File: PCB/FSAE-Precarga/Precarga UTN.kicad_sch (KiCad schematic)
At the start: 64 parts, among them J1 TS+, J3 Conn_02x05_Counter_Clockwise, J4 Conn_01x02_Pin, J5 RA+_Control, J6 RA-_Control, J7 TS-, SW1 SW_MEC_5E, U1 TMA-1212S, U2 LM331N, U3 6N137, U4 6N137, U5 LM331N, U6 STM32F103C8Tx, U7 LM1117DT-3.3, Y1 Crystal

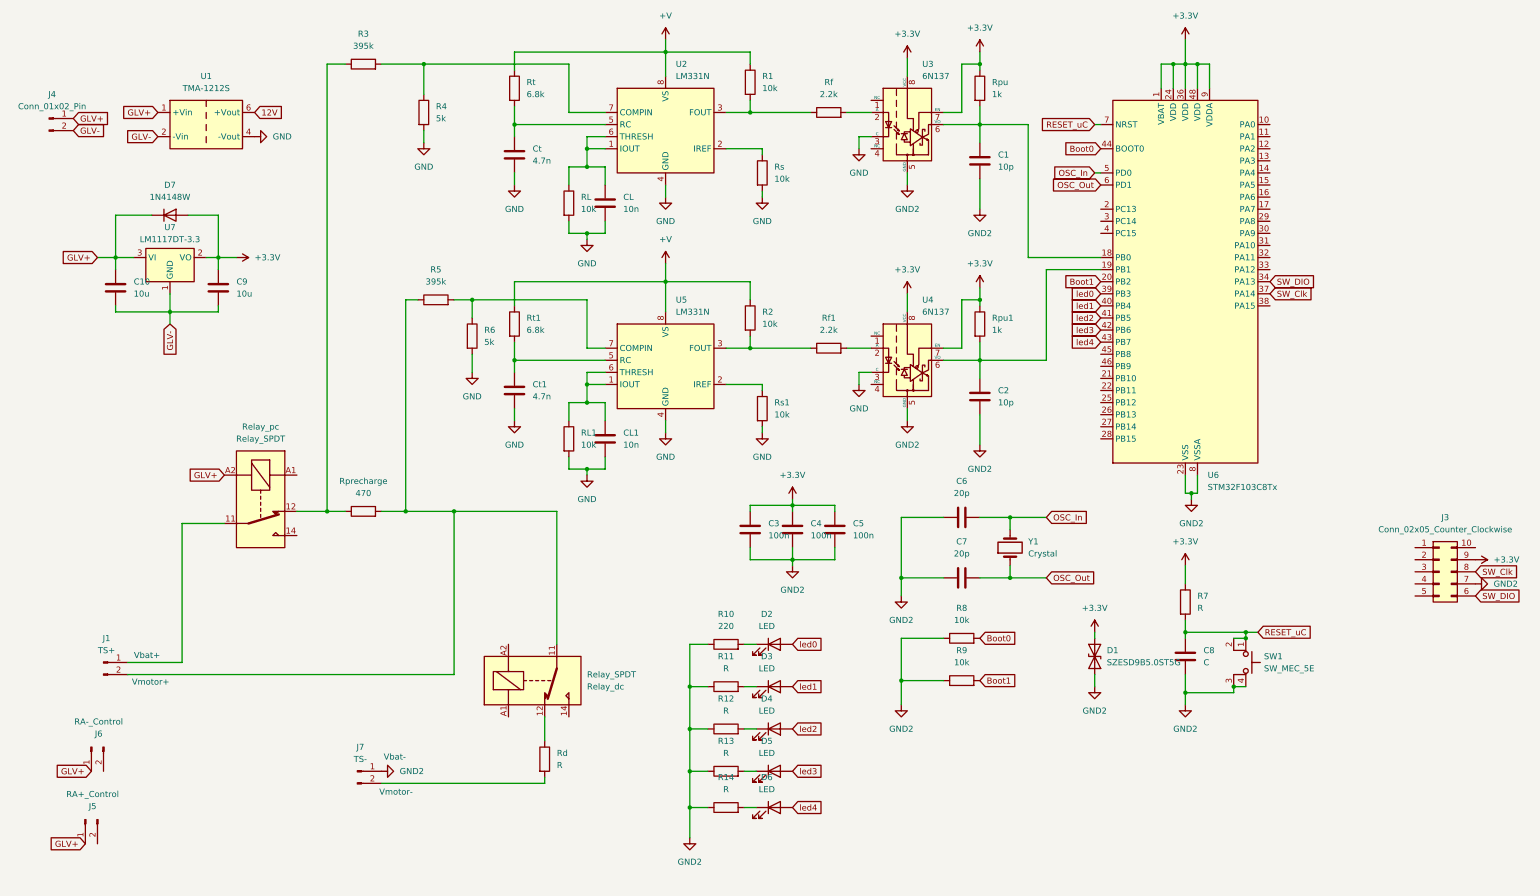
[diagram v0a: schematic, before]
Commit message: Version avanzada (NO final) de la placa de precarga
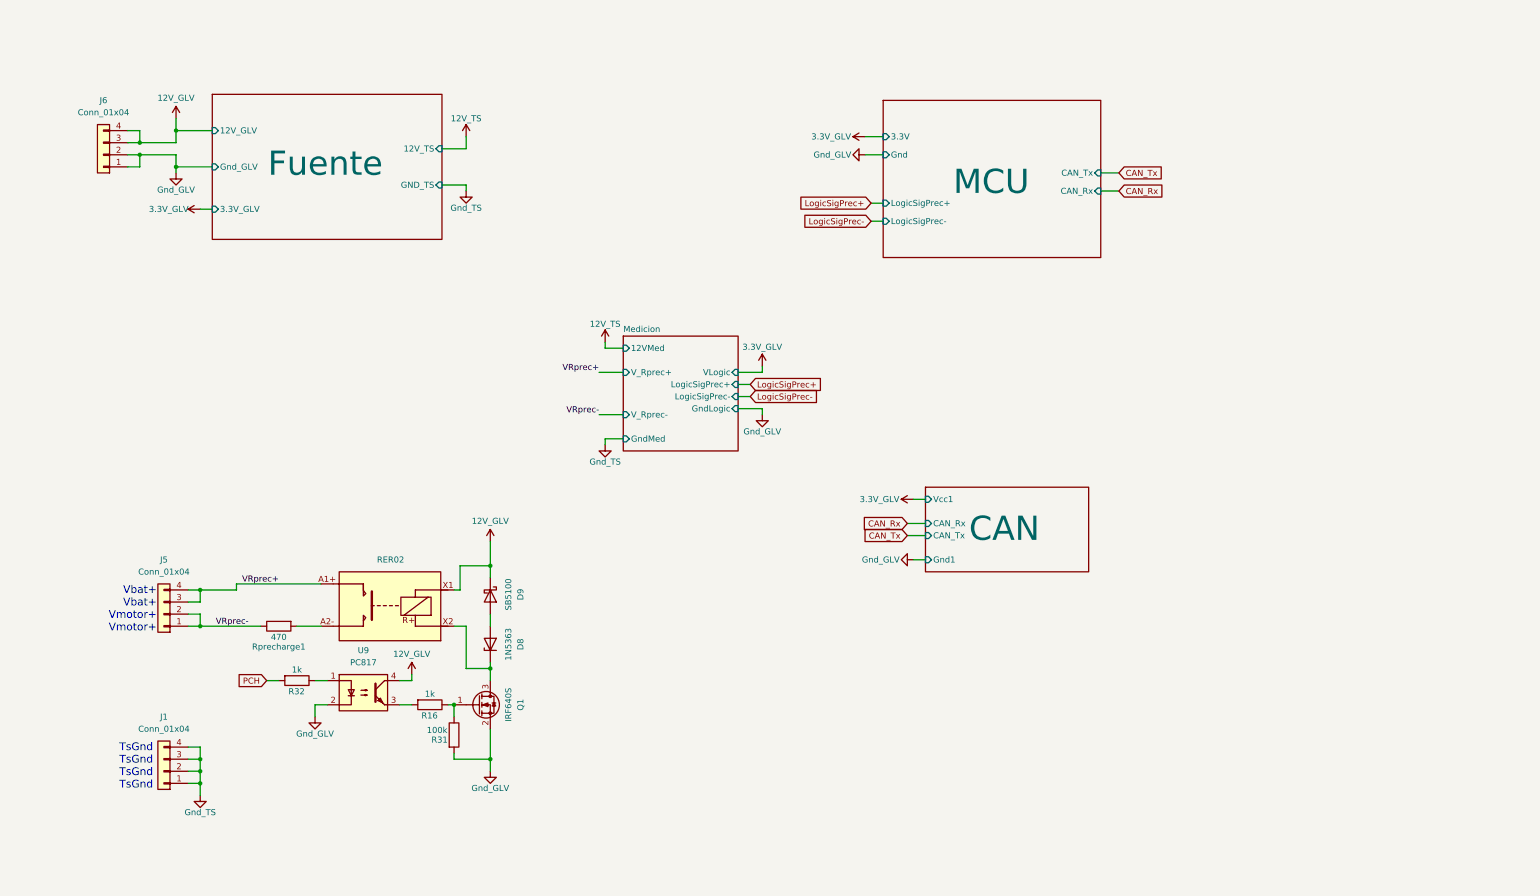
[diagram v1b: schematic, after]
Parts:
- removed C1, C2: 10p, symbol Device:C
- removed C10, C9: 10u, symbol Device:C
- removed C3, C4, C5: 100n, symbol Device:C
- removed C6, C7: 20p, symbol Device:C
- removed C8: C, symbol Device:C
- removed CL, CL1: 10n, symbol Device:C
- removed Ct, Ct1: 4.7n, symbol Device:C
- removed D1: SZESD9B5.0ST5G, Diode_SMD:D_SOD-923, symbol Diode:SZESD9B5.0ST5G
- removed D2, D3, D4, D5, D6: LED, symbol Device:LED
- removed D7: 1N4148W, Diode_SMD:D_SOD-123, symbol Diode:1N4148W
- removed J1: TS+, symbol Connector:Conn_01x02_Pin
- removed J3: Conn_02x05_Counter_Clockwise, Connector_IDC:IDC-Header_2x05_P2.54mm_Vertical, symbol Connector_Generic:Conn_02x05_Counter_Clockwise
- removed J4: Conn_01x02_Pin, symbol Connector:Conn_01x02_Pin
- removed J5: RA+_Control, symbol Connector:Conn_01x02_Pin
- removed J6: RA-_Control, symbol Connector:Conn_01x02_Pin
- removed J7: TS-, symbol Connector:Conn_01x02_Pin
- removed R1, R2, R8, R9, RL, RL1, Rs, Rs1: 10k, symbol Device:R
- removed R10: 220, symbol Device:R
- removed R11, R12, R13, R14, R7, Rd: R, symbol Device:R
- removed R3, R5: 395k, symbol Device:R
- removed R4, R6: 5k, symbol Device:R
- removed Relay_dc, Relay_pc: Relay_SPDT, symbol Relay:Relay_SPDT
- removed Rf, Rf1: 2.2k, symbol Device:R
- removed Rpu, Rpu1: 1k, symbol Device:R
- removed Rt, Rt1: 6.8k, symbol Device:R
- removed SW1: SW_MEC_5E, symbol Switch:SW_MEC_5E
- removed U1: TMA-1212S, Converter_DCDC:Converter_DCDC_TRACO_TMA-05xxS_12xxS_Single_THT, symbol Converter_DCDC:TMA-1212S
- removed U2, U5: LM331N, Package_DIP:SMDIP-8_W7.62mm, symbol Analog:LM331N
- removed U3, U4: 6N137, Package_DIP:SMDIP-8_W7.62mm, symbol Isolator:6N137
- removed U6: STM32F103C8Tx, Package_QFP:LQFP-48_7x7mm_P0.5mm, symbol MCU_ST_STM32F1:STM32F103C8Tx
- removed U7: LM1117DT-3.3, Package_TO_SOT_SMD:TO-252-2, symbol Regulator_Linear:LM1117DT-3.3
- removed Y1: Crystal, symbol Device:Crystal
- added D8: 1N5363, Diode_THT:D_DO-41_SOD81_P10.16mm_Horizontal, symbol Diode:1N53xxB
- added D9: SB5100, Diode_THT:D_DO-41_SOD81_P10.16mm_Horizontal, symbol Diode:SB5H100
- added J1, J5, J6: Conn_01x04, GeneratedConnector:Molex_Mini50, symbol Connector_Generic:Conn_01x04
- added K1: RER02, Mis_Huellas:RER02PAX, symbol MisSimbolos:RER02-Series
- added Q1: IRF640S, Package_TO_SOT_SMD:TO-263-2, symbol Transistor_FET:AO3400A
- added R16, R32: 1k, Resistor_SMD:R_0603_1608Metric, symbol Device:R
- added R31: 100k, Resistor_SMD:R_0603_1608Metric, symbol Device:R
- added U9: PC817, Package_DIP:DIP-4_W7.62mm_SMDSocket_SmallPads, symbol Isolator:PC817
- Rprecharge1: renamed from Rprecharge; PaginaProveedor (none) -> https://www.digikey.com/es/products/detail/ohmite/HS25-470R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
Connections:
- net VRprec-: now reaches Rprecharge1.1
- net VRprec-: now also J5.1 (Pin_1), J5.2 (Pin_2)
- net at Rprecharge1.2: now also K1.A2-
- new net: D8.1 (K), K1.X2, Q1.3 (D)
- new net: D8.2 (A), D9.2 (A)
- new net: R32.1, U9.1
- new net: Q1.1 (G), R16.1, R31.1
- new net: R16.2, U9.3
- new net 12V_GLV: D9.1 (K), J6.3 (Pin_3), J6.4 (Pin_4), K1.X1, U9.4
- new net Gnd_GLV: J6.1 (Pin_1), J6.2 (Pin_2), Q1.2 (S), R31.2, U9.2
- new net Gnd_TS: J1.1 (Pin_1), J1.2 (Pin_2), J1.3 (Pin_3), J1.4 (Pin_4)
- new net PCH: R32.2
- new net VRprec+: J5.3 (Pin_3), J5.4 (Pin_4), K1.A1+
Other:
- added sheet CAN (CANModule.kicad_sch)
- added sheet Fuente (Fuente.kicad_sch)
- added sheet MCU (mcu.kicad_sch)
- added sheet Medicion (Medicion.kicad_sch)
- note added: "TsGnd TsGnd TsGnd TsGnd"
- note added: "Vbat+ Vbat+ Vmotor+ Vmotor+"
- note removed: "Vbat+"
- note removed: "Vbat-"
- note removed: "Vmotor+"
- note removed: "Vmotor-"
- company: (none) -> UTN-FRBA-FSAE
- title: (none) -> SistemaCarga
- moved on the sheet: Rprecharge1

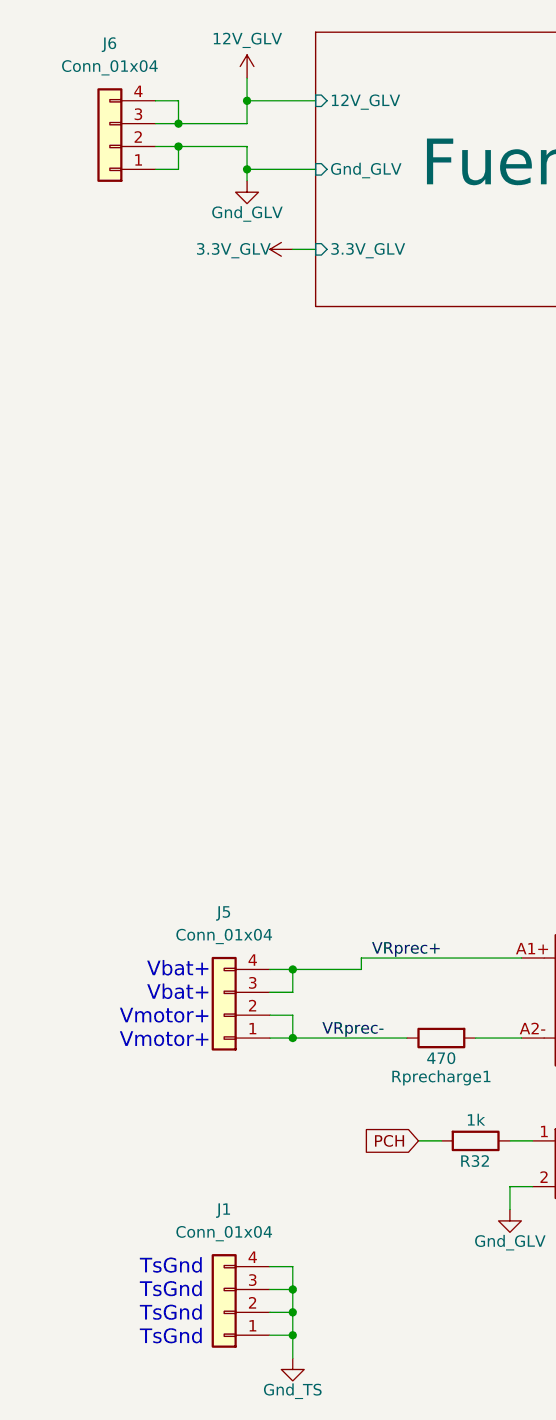
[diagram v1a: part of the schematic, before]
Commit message: Version avanzada de la placa de Precarga
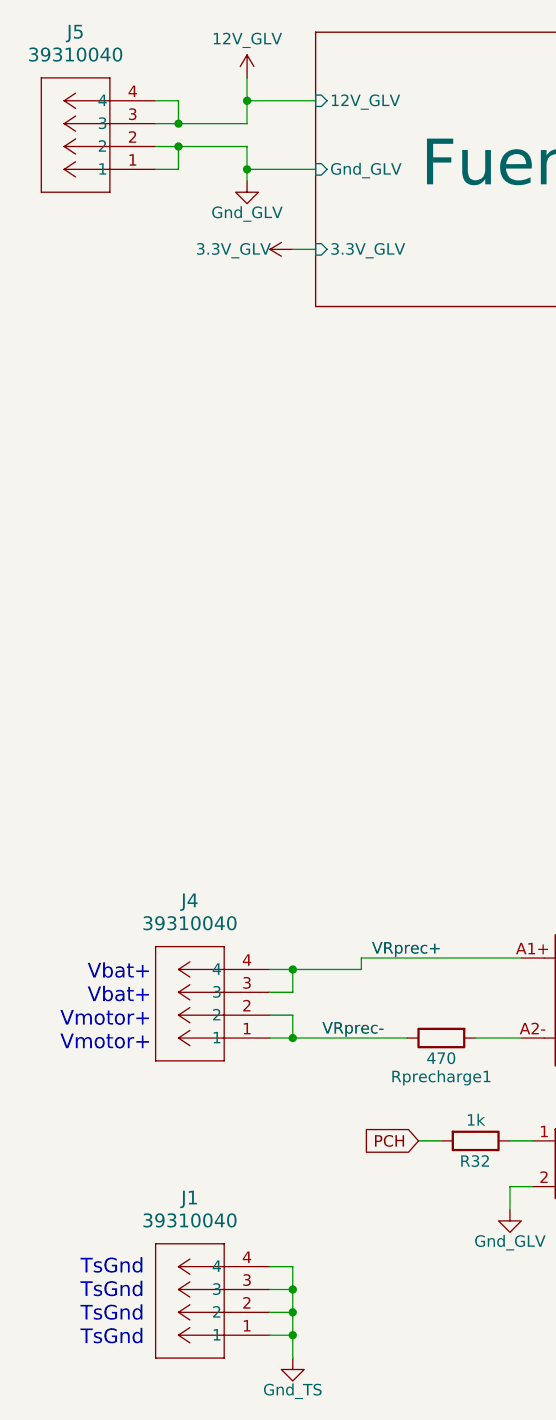
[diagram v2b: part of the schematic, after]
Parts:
- removed J1, J5, J6: Conn_01x04, GeneratedConnector:Molex_Mini50, symbol Connector_Generic:Conn_01x04
- added J1, J4, J5: 39310040, CONN_SD-5566-002_04_MOL, symbol 2026-08-15_23-43-52:39310040
- Rprecharge1: JLCPart (none) -> HS25 470R F
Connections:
- net 12V_GLV: now also J5.3, J5.4
- net Gnd_GLV: now also J5.1, J5.2
- net Gnd_TS: now also J1.1, J1.2, J1.3, J1.4
- net VRprec+: now also J4.3, J4.4
- net VRprec-: now also J4.1, J4.2

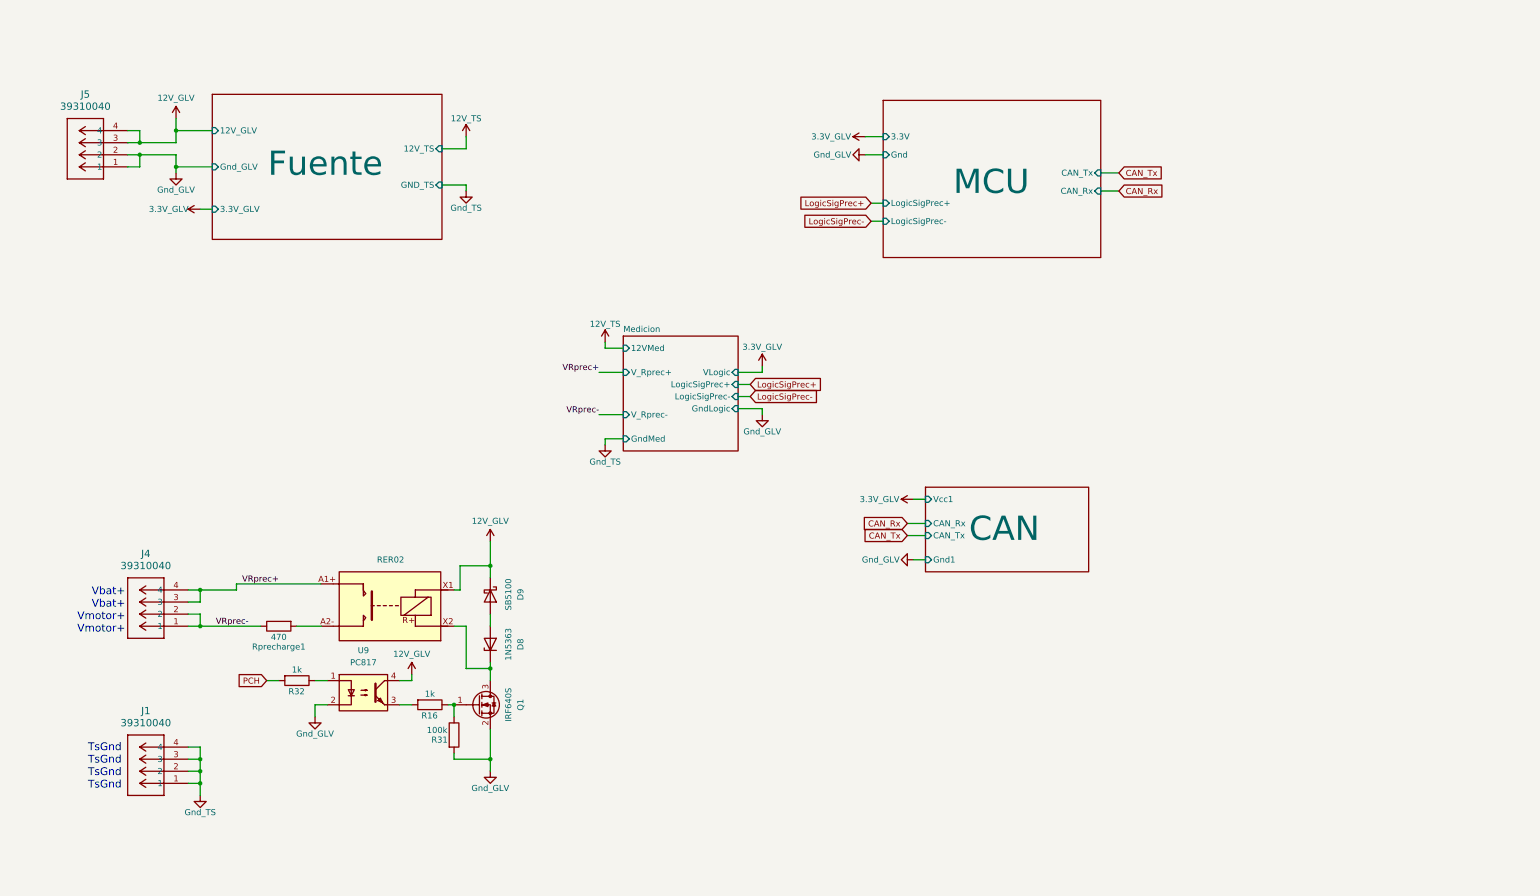
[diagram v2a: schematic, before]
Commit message: Agrego correcciones/agregados placa precarga
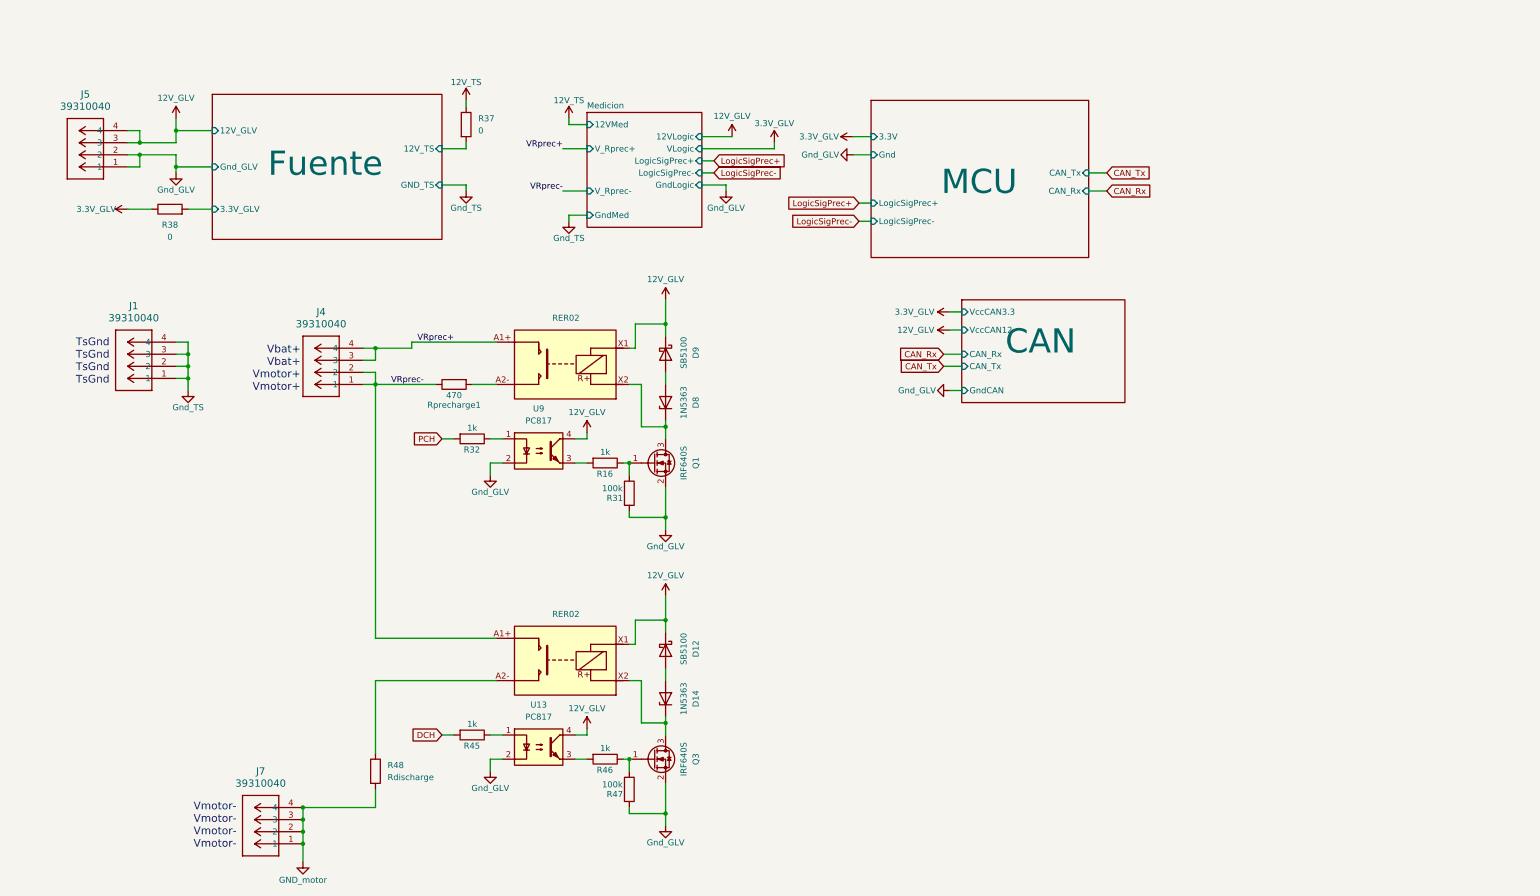
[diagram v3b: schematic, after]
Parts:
- added D12: SB5100, Diode_THT:D_DO-41_SOD81_P10.16mm_Horizontal, symbol Diode:SB5H100
- added D14: 1N5363, Diode_THT:D_DO-41_SOD81_P10.16mm_Horizontal, symbol Diode:1N53xxB
- added J7: 39310040, CONN_SD-5566-002_04_MOL, symbol 2026-08-15_23-43-52:39310040
- added K2: RER02, Mis_Huellas:RER02PAX, symbol MisSimbolos:RER02-Series
- added Q3: IRF640S, Package_TO_SOT_SMD:TO-263-2, symbol Transistor_FET:AO3400A
- added R37, R38: 0, Resistor_SMD:R_0805_2012Metric, symbol Device:R
- added R45, R46: 1k, Resistor_SMD:R_0603_1608Metric, symbol Device:R
- added R47: 100k, Resistor_SMD:R_0603_1608Metric, symbol Device:R
- added R48: Rdischarge, symbol Device:R
- added U13: PC817, Package_DIP:DIP-4_W7.62mm_SMDSocket_SmallPads, symbol Isolator:PC817
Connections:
- net 12V_GLV: now also D12.1 (K), K2.X1, U13.4
- net 12V_TS: now also R37.1
- net 3.3V_GLV: now also R38.1
- net Gnd_GLV: now also Q3.2 (S), R47.2, U13.2
- net VRprec-: now also K2.A1+
- new net: Q3.1 (G), R46.1, R47.1
- new net: D14.1 (K), K2.X2, Q3.3 (D)
- new net: R45.1, U13.1
- new net: D12.2 (A), D14.2 (A)
- new net: K2.A2-, R48.1
- new net: R46.2, U13.3
- new net DCH: R45.2
- new net Fuente/12V_TS: R37.2
- new net Fuente/3.3V_GLV: R38.2
- new net GND_motor: J7.1, J7.2, J7.3, J7.4, R48.2
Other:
- sheet CAN ports: added GndCAN, VccCAN12, VccCAN3.3; removed Gnd1, Vcc1
- sheet Medicion ports: added 12VLogic; removed none
- note added: "Vmotor- Vmotor- Vmotor- Vmotor-"
- moved on the sheet: D8, D9, J1, J4, Q1, R16, R31, R32, Rprecharge1, U9
